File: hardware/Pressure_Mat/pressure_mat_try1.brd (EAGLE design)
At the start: 160 x 100 mm, 34 parts, among them IC1 MCP23017T-E_ML, U1 MUX-74HC4067

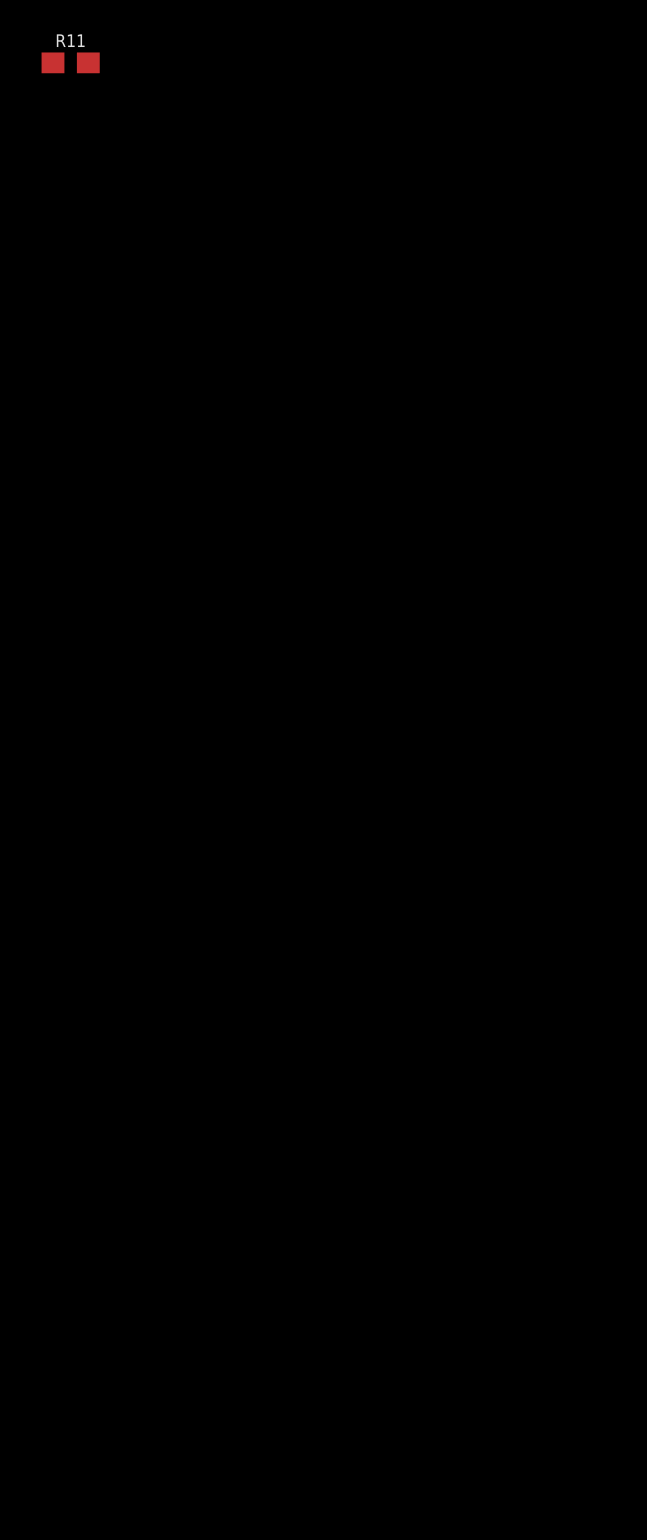
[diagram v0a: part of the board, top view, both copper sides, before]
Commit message: Uploaded new Eagle schematic and board
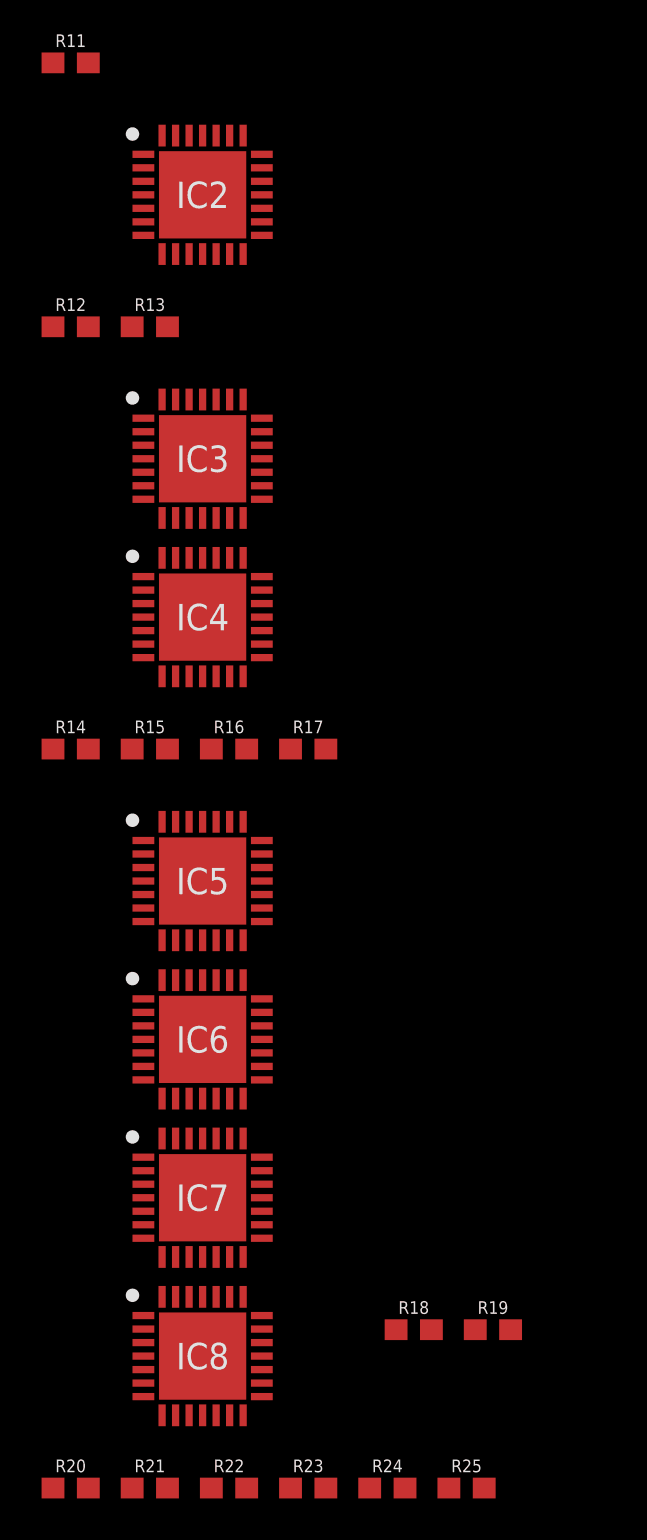
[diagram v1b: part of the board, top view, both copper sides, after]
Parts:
- added IC2, IC3, IC4, IC5, IC6, IC7, IC8: MCP23017T-E_ML, SamacSys_Parts:QFN65P600X600X100-29N
- added R12, R13, R14, R15, R16, R17, R18, R19, R20, R21, R22, R23, R24, R25: 4.7k, SparkFun-Resistors:0603
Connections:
- new net PIN_3: IC1.15, IC2.15, IC3.15, IC4.15, IC5.15, IC6.15, IC7.15, IC8.15
- net GND: now also IC2.12, IC2.13, IC2.6, IC3.11, IC3.13, IC3.6, IC4.13, IC4.6, IC5.11, IC5.12, IC5.6, IC6.12, IC6.6, IC7.11, IC7.6, IC8.6
- net I2C$SCL: now also IC2.8, IC3.8, IC4.8, IC5.8, IC6.8, IC7.8, IC8.8, R13.2, R15.2, R17.2, R19.2, R21.2, R23.2, R25.2
- net I2C$SDA: now also IC2.9, IC3.9, IC4.9, IC5.9, IC6.9, IC7.9, IC8.9, R12.2, R14.2, R16.2, R18.2, R20.2, R22.2, R24.2
- net P$1: now also IC1.17
- net P$10: now also IC1.26
- net P$100: now also IC7.20
- net P$101: now also IC7.21
- net P$102: now also IC7.22
- net P$103: now also IC7.23
- net P$104: now also IC7.24
- net P$105: now also IC7.25
- net P$106: now also IC7.26
- net P$107: now also IC7.27
- net P$108: now also IC7.28
- net P$109: now also IC7.1
- net P$11: now also IC1.27
- net P$110: now also IC7.2
- net P$111: now also IC7.3
- net P$112: now also IC7.4
- net P$113: now also IC8.17
- net P$114: now also IC8.18
- net P$115: now also IC8.19
- net P$116: now also IC8.20
- net P$117: now also IC8.21
- net P$118: now also IC8.22
- net P$119: now also IC8.23
- net P$12: now also IC1.28
- net P$120: now also IC8.24
- net P$121: now also IC8.25
- net P$122: now also IC8.26
- net P$123: now also IC8.27
- net P$124: now also IC8.28
- net P$125: now also IC8.1
- net P$126: now also IC8.2
- net P$127: now also IC8.3
- net P$128: now also IC8.4
- net P$13: now also IC1.1
- net P$14: now also IC1.2
- net P$15: now also IC1.3
- net P$16: now also IC1.4
- net P$17: now also IC2.17
- net P$18: now also IC2.18
- net P$19: now also IC2.19
- net P$2: now also IC1.18
- net P$20: now also IC2.20
- net P$21: now also IC2.21
- net P$22: now also IC2.22
- net P$23: now also IC2.23
- net P$24: now also IC2.24
- net P$25: now also IC2.25
- net P$26: now also IC2.26
- net P$27: now also IC2.27
- net P$28: now also IC2.28
- net P$29: now also IC2.1
- net P$3: now also IC1.19
- net P$30: now also IC2.2
- net P$31: now also IC2.3
- net P$32: now also IC2.4
- net P$33: now also IC3.17
- net P$34: now also IC3.18
- net P$35: now also IC3.19
- net P$36: now also IC3.20
- net P$37: now also IC3.21
- net P$38: now also IC3.22
- net P$39: now also IC3.23
- net P$4: now also IC1.20
- net P$40: now also IC3.24
- net P$41: now also IC3.25
- net P$42: now also IC3.26
- net P$43: now also IC3.27
- net P$44: now also IC3.28
- net P$45: now also IC3.1
- net P$46: now also IC3.2
- net P$47: now also IC3.3
- net P$48: now also IC3.4
- net P$49: now also IC4.17
- net P$5: now also IC1.21
- net P$50: now also IC4.18
- net P$51: now also IC4.19
- net P$52: now also IC4.20
- net P$53: now also IC4.21
- net P$54: now also IC4.22
- net P$55: now also IC4.23
- net P$56: now also IC4.24
- net P$57: now also IC4.25
- net P$58: now also IC4.26
- net P$59: now also IC4.27
- net P$6: now also IC1.22
- net P$60: now also IC4.28
- net P$61: now also IC4.1
- net P$62: now also IC4.2
- net P$63: now also IC4.3
- net P$64: now also IC4.4
- net P$65: now also IC5.17
- net P$66: now also IC5.18
- net P$67: now also IC5.19
- net P$68: now also IC5.20
- net P$69: now also IC5.21
- net P$7: now also IC1.23
- net P$70: now also IC5.22
- net P$71: now also IC5.23
- net P$72: now also IC5.24
- net P$73: now also IC5.25
- net P$74: now also IC5.26
- net P$75: now also IC5.27
- net P$76: now also IC5.28
- net P$77: now also IC5.1
- net P$78: now also IC5.2
- net P$79: now also IC5.3
- net P$8: now also IC1.24
- net P$80: now also IC5.4
- net P$81: now also IC6.17
- net P$82: now also IC6.18
- net P$83: now also IC6.19
- net P$84: now also IC6.20
- net P$85: now also IC6.21
- net P$86: now also IC6.22
- net P$87: now also IC6.23
- net P$88: now also IC6.24
- net P$89: now also IC6.25
- net P$9: now also IC1.25
- net P$90: now also IC6.26
- net P$91: now also IC6.27
- net P$92: now also IC6.28
- net P$93: now also IC6.1
- net P$94: now also IC6.2
- net P$95: now also IC6.3
- net P$96: now also IC6.4
- net P$97: now also IC7.17
- net P$98: now also IC7.18
- net P$99: now also IC7.19
- net VCC: now also IC2.11, IC2.14, IC2.5, IC3.12, IC3.14, IC3.5, IC4.11, IC4.12, IC4.14, IC4.5, IC5.13, IC5.14, IC5.5, IC6.11, IC6.13, IC6.14, IC6.5, IC7.12, IC7.13, IC7.14, IC7.5, IC8.11, IC8.12, IC8.13, IC8.14, IC8.5, R12.1, R13.1, R14.1, R15.1, R16.1, R17.1, R18.1, R19.1, R20.1, R21.1, R22.1, R23.1, R24.1, R25.1
